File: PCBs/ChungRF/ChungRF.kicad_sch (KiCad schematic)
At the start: 11 parts, among them J1 Conn_Coaxial, J2 Conn_01x09_Socket, U1 E22-900M30S

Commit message: Rename to ChungRF
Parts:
- added C1: 100nF, Capacitor_SMD:C_0603_1608Metric, symbol Device:C
- added C2: 1uF, Capacitor_SMD:C_0603_1608Metric, symbol Device:C
- added R1, R2: 100k, Capacitor_SMD:C_0603_1608Metric, symbol Device:R
- J2: footprint Connector_JST:JST_GH_BM09B-GHS-TBT_1x09-1MP_P1.25mm_Vertical -> Connector_JST:JST_SH_SM09B-SRSS-TB_1x09-1MP_P1.00mm_Horizontal
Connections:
- net BUSY: now also J2.8 (Pin_8); no longer J2.2 (Pin_2)
- net DIO1: now also J2.9 (Pin_9); no longer J2.1 (Pin_1)
- net GND: now also J2.2 (Pin_2), C1.2, C2.2, R1.1, R2.2; no longer J2.8 (Pin_8)
- net MISO: now also J2.6 (Pin_6); no longer J2.4 (Pin_4)
- net NRST: now also J2.7 (Pin_7); no longer J2.3 (Pin_3)
- net NSS: now also J2.3 (Pin_3); no longer J2.7 (Pin_7)
- net RXEN: now also R1.2
- net SCK: now also J2.4 (Pin_4); no longer J2.6 (Pin_6)
- net TXEN: now also R2.1
- net VCC: now also J2.1 (Pin_1), C1.1, C2.1; no longer J2.9 (Pin_9)
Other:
- moved on the sheet: J2

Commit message: Update ChungRF
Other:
- moved on the sheet: C1, C2, H1, H2, H3, J1, J2, R1, R2, TP1, TP2, TP3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

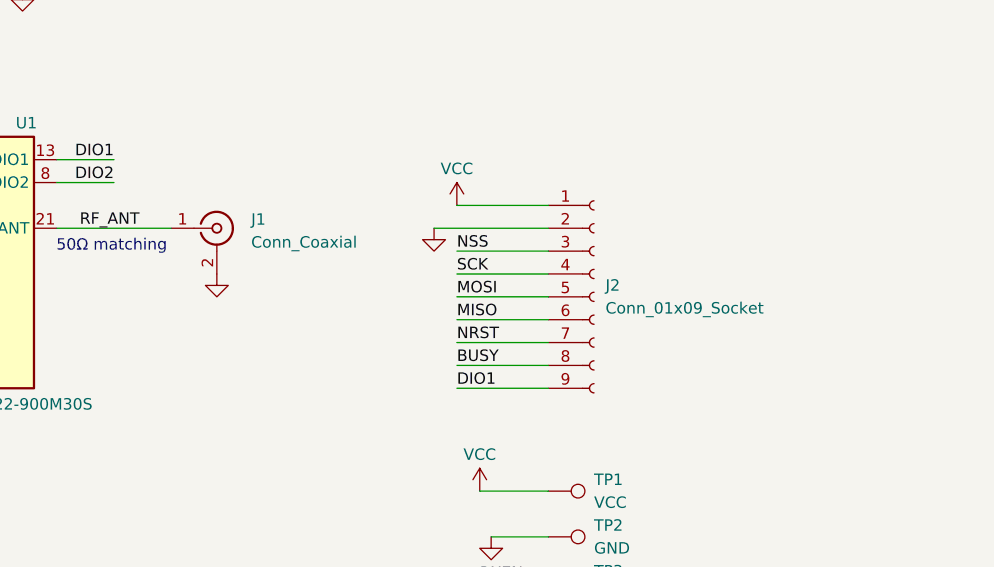
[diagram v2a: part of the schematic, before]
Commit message: Fix impedance
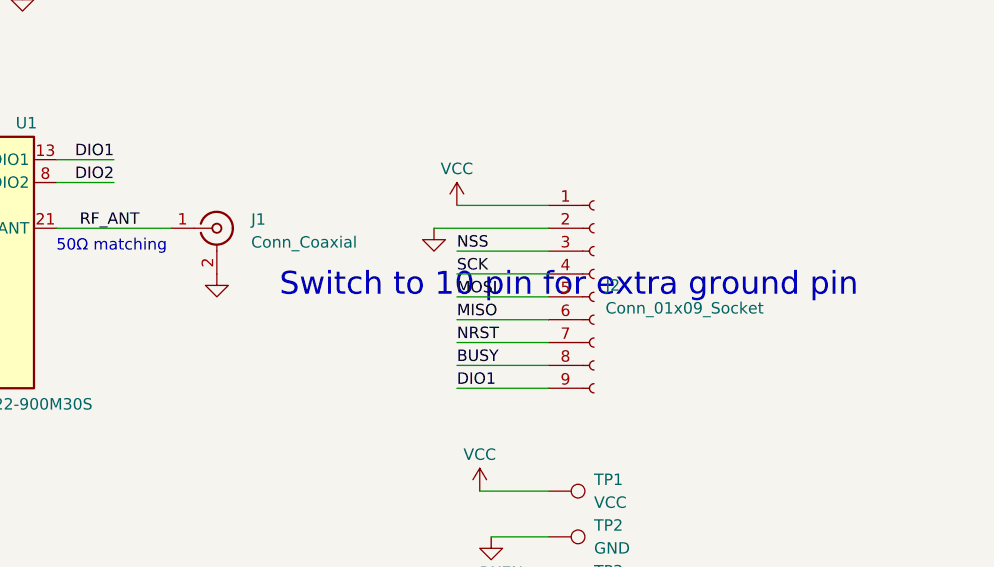
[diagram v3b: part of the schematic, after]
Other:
- note added: "Switch to 10 pin for extra ground pin"
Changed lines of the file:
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@@
+		)
+	)
+	(text "Switch to 10 pin for extra ground pin"
+		(exclude_from_sim no)
+		(at 188.976 88.9 0)
+		(effects
+			(font
+				(size 2.54 2.54)
+			)
 		)
 	)

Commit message: Finalize design, add gerbers
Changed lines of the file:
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@@
 	(text "Switch to 10 pin for extra ground pin"
 		(exclude_from_sim no)
-		(at 188.976 88.9 0)
+		(at 192.532 70.612 0)
 		(effects
 			(font
@@
 				)
 				(justify left)
+				(hide yes)
 			)
 		)
@@
 			)
 		)
-		(property "Datasheet" " ~"
+		(property "Datasheet" "https://www.digikey.com/en/products/detail/rf-solutions/CON-SMA-EDGE-S/5845767"
 			(at 149.86 82.55 0)
 			(effects

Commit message: Update ChungRF, add software tests
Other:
- title: Ebyte E22 Radio Breakout -> ChungRF
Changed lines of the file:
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@@
 	(paper "A4")
 	(title_block
-		(title "Ebyte E22 Radio Breakout")
-		(date "2024-05-13")
-		(rev "R1")
+		(title "ChungRF")
+		(date "2024-05-23")
+		(rev "R2")
 		(company "Chungus Aerospace")
 	)
@@
 		(dnp no)
 		(property "Reference" "R2"
-			(at 96.52 88.9 90)
+			(at 96.52 88.9 0)
 			(effects
 				(font
@@
 		(dnp no)
 		(property "Reference" "R1"
-			(at 88.9 86.36 90)
-			(effects
-				(font
+			(at 88.9 86.36 0)
+			(effects
+				(font

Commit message: ChungRF R2
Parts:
- removed H3: MountingHole, MountingHole:MountingHole_2.7mm_M2.5_Pad_Via, symbol Mechanical:MountingHole
- removed J2: Conn_01x09_Socket, Connector_JST:JST_SH_SM09B-SRSS-TB_1x09-1MP_P1.00mm_Horizontal, symbol Connector:Conn_01x09_Socket
- removed TP1: VCC, TestPoint:TestPoint_Pad_D1.5mm, symbol Connector:TestPoint
- removed TP2: GND, TestPoint:TestPoint_Pad_D1.5mm, symbol Connector:TestPoint
- removed TP3: RXEN, TestPoint:TestPoint_Pad_D1.5mm, symbol Connector:TestPoint
- removed TP4: TXEN, TestPoint:TestPoint_Pad_D1.5mm, symbol Connector:TestPoint
- removed TP5: DIO2, TestPoint:TestPoint_Pad_D1.5mm, symbol Connector:TestPoint
- added C3: 10uF, Capacitor_SMD:C_0603_1608Metric, symbol Device:C
- added J1: JST-SM04B-SRSS, besser_footprints:JST_SH_SM04B-SRSS-TB_1x04-1MP_P1.00mm_Horizontal, symbol Connector:Conn_01x04_Socket
- added U1: KB2040, besser_footprints:Adafuit-KB2040-SMD, symbol besserLib:Adafruit-KB2040
- H1, H2: value MountingHole -> 2.7mm_M2.5_Pad_Via
- J2: renamed from J1; footprint besser_footprints:CON-SMA-EDGE-S -> besser_footprints:CONSMA003.062
- R1, R2: value 100k -> 10k
- renumbered U1 to U2
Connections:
- net BUSY: now also U1.19 (A1)
- net DIO1: now also U1.20 (A2)
- net DIO2: now also U1.7 (D3)
- net GND: now also C3.2, J1.1 (Pin_1), U1.24 (GND), U1.4 (GND), U1.5 (GND)
- net MISO: now also U1.17 (SCK)
- net MOSI: now also U1.16 (MISO)
- net NRST: now also U1.18 (A0)
- net NSS: now also U1.14 (D10)
- net SCK: now also U1.15 (MOSI)
- net VCC renamed VBUS
- net VBUS: now also C3.1, J1.2 (Pin_2), U1.25 (RAW)
- new net CARFIO_MISO: J1.3 (Pin_3), U1.3 (D1)
- new net CARFIO_MOSI: J1.4 (Pin_4), U1.2 (D0)
- no-connect marks 0 -> 12
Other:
- note added: "IO Conn."
- note added: "MCU"
- note added: "No protection against USB and CARFIO power. Only plug one in at a time."
- note added: "Pins connections do not follow convention for easier routing."
- note added: "Radio"
- note removed: "Switch to 10 pin for extra ground pin"
- moved on the sheet: C1, C2, J2, R1, R2

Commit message: ChungRF R3
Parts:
- R1, R2: now not fitted
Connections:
- net BUSY: now also U1.9 (D5); no longer U1.19 (A1)
- net DIO1: now also U1.6 (D2); no longer U1.20 (A2)
- net MISO: now also U1.16 (MISO); no longer U1.17 (SCK)
- net MOSI: now also U1.15 (MOSI); no longer U1.16 (MISO)
- net NRST: now also U1.8 (D4); no longer U1.18 (A0)
- net NSS: now also U1.7 (D3); no longer U1.14 (D10)
- net SCK: now also U1.17 (SCK); no longer U1.15 (MOSI)
- net CARFIO_MISO renamed CARFIO_SDA
- net CARFIO_MOSI renamed CARFIO_SCL
- net DIO2: no longer names the net of U2.8 (DIO2)
- net DIO2: no longer U1.7 (D3)
- no-connect marks 12 -> 14
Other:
- note added: "CARFIO Con."
- note added: "Pin layout is bad for routing, but it works. Do NOT change them."
- note added: "VBUS == 5v 800mA"
- note removed: "IO Conn."
- note removed: "Pins connections do not follow convention for easier routing."
- moved on the sheet: U1

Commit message: Clean Tracks, add Gerber files
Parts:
- removed R1, R2: 10k, Capacitor_SMD:C_0603_1608Metric, symbol Device:R
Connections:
- net NSS: now also U1.11 (D7); no longer U1.7 (D3)
- net RXEN: now also U1.13 (D9)
- net TXEN: now also U1.12 (D8)
- no-connect marks 14 -> 12
